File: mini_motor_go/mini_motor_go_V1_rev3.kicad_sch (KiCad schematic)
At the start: 30 parts, among them J10 Conn_01x02_Pin, J11 USB4520-03-0-A_REVA, J12 BM05B-SRSS-TB_LF__SN_, J13 BM05B-SRSS-TB_LF__SN_, J3 I2C_STANDARDQWIIC, J5 I2C_STANDARDQWIIC, J9 Conn_01x09_Pin, U1 ESP32-S3-WROOM-1

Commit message: added part numbers and links to most parts. Ready for review. -TS
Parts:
- D1, D2, D3: LCSC Part Number (none) -> C965812; Manufacturer_Name (none) -> XINGLIGHT; Manufacturer_Part_Number (none) -> XL-2012SURC; note (none) -> not sure what "~" means. added P/N in case needed.
- J10: note (none) -> 2 pin GPIO? is there a P/N to specify for this? 1x2 2.54mm 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
- J11: LCSC Part Number (none) -> n/a; Manufacturer_Name (none) -> GCT; Manufacturer_Part_Number (none) -> USB4520-03-0-A; note (none) -> no LCSC P/N. didn't see replacement in LCSC. recommend for 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
- J12, J13: LCSC Part Number (none) -> C268096; Manufacturer_Name (none) -> JST; Manufacturer_Part_Number (none) -> SM05B-NSHSS-TB(LF)(SN); note (none) -> JST 5 pin for encoders. recommend confirming this is right.
- J3, J5: LCSC Part Number (none) -> C160404; Manufacturer_Name (none) -> JST; Manufacturer_Part_Number (none) -> SM04B-SRSS-TB(LF)(SN); note (none) -> This looks like JST 4 pin. recommend confirming.
- J6, J7: LCSC Part Number (none) -> C2800385; Manufacturer_Name (none) -> C&K; Manufacturer_Part_Number (none) -> PTS526 SM08 SMTR2 LFS; note (none) -> SMD buttons.
- J9: LCSC Part Number (none) -> C6332202; Manufacturer_Name (none) -> Hanbo Electronic; Manufacturer_Part_Number (none) -> HB-PH3-25419PB2GOP; note (none) -> 9 pin GPIO? Do we need to specify? added one in case.
- JP1, JP2, JP3: note (none) -> function unclear. looks like a pad of solder. P/N needed?
- R20, R21: LCSC Part Number (none) -> C2906858; Manufacturer_Name (none) -> FOJAN; Manufacturer_Part_Number (none) -> FRC0402F0000TS; note (none) -> 1%, 62.5 mW thick film chip resistor.
- R22, R32, R33: LCSC Part Number (none) -> C3015791; Manufacturer_Name (none) -> VO; Manufacturer_Part_Number (none) -> SCR0402F1K; note (none) -> 1%. see R3-R14. same part selection.
- R23, R24, R25, R26, R27, R28, R29, R30, R31: LCSC Part Number (none) -> C100461; Manufacturer_Name (none) -> LIZ Elec; Manufacturer_Part_Number (none) -> CR0402FF5101G; note (none) -> 1%. 62.5 mW. thick film resistor. 50V overload voltage.
- U1: LCSC Part Number (none) -> C2913198; Manufacturer_Name (none) -> Espressif Systems; Manufacturer_Part_Number (none) -> ESP32-S3-WROOM-1-N8; note (none) -> insufficient detail to fully specify in LCSC. Chose N8 base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

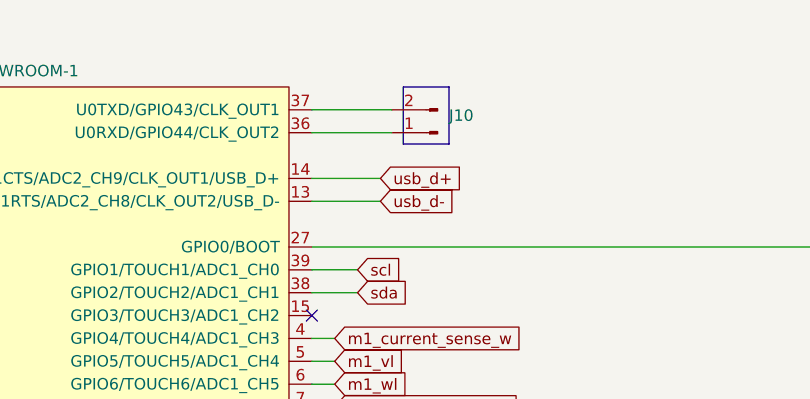
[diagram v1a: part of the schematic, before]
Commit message: reviewed value table in schematics, updated footprints on board minor improvements
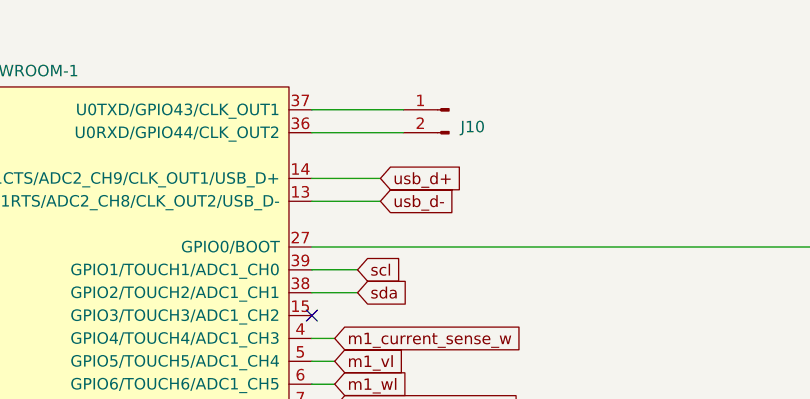
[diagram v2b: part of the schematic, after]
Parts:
- D1, D2, D3: note not sure what "~" means. added P/N in case needed. -> consider select different colors for each
- J10: note 2 pin GPIO? is there a P/N to specify for this? 1x2 2.54mm 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 -> this one is odd, but we are combining j9 and j10 into one 1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
- J11: note no LCSC P/N. didn't see replacement in LCSC. recommend for 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 -> from last order we used: C2965608
- J12, J13: note JST 5 pin for encoders. recommend confirming this is right. -> (none)
- J3, J5: note This looks like JST 4 pin. recommend confirming. -> (none)
- J6, J7: note SMD buttons. -> use button part sent in engineering channel
- J9: note 9 pin GPIO? Do we need to specify? added one in case. -> this one is odd, but we are combining j9 and j10 into one 1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
- JP1, JP2, JP3: note function unclear. looks like a pad of solder. P/N needed? -> DNP
- R20, R21: note 1%, 62.5 mW thick film chip resistor. -> (none)
- R22, R32, R33: note 1%. see R3-R14. same part selection. -> (none)
- R23, R24, R25, R26, R27, R28, R29, R30, R31: note 1%. 62.5 mW. thick film resistor. 50V overload voltage. -> (none)
- U1: note insufficient detail to fully specify in LCSC. Chose N8 base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 -> (none)
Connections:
- net at U1.36 (U0RXD/GPIO44/CLK_OUT2): now also J10.2 (Pin_2); no longer J10.1 (Pin_1)
- net at U1.37 (U0TXD/GPIO43/CLK_OUT1): now also J10.1 (Pin_1); no longer J10.2 (Pin_2)
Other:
- moved on the sheet: J10
